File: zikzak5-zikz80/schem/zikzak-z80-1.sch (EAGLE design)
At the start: 3 parts, among them IC1 Z80, IC3 MC6850

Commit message: basic z80 schematic nearly done (missing video and atmega basics like xtal etc)
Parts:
- added BUFFER3: 74LS245N, 74xx-us:74LS245N
- added C1, C2: 0.1uF, SparkFun:CAP0402-CAP
- added C3: (no value), rcl:C-EU025-050X050
- added C4, C6: (no value), rcl:C-EUC0504
- added C5: 10uF, SparkFun:CAP_POL1206
- added IC10, IC11, IC12, IC13, IC15, IC4, IC6: 74LS32N, 74xx-us:74LS32N
- added IC14, IC5, IC7, IC8, IC9: 74LS04N, 74xx-us:74LS04N
- added IC2: ATMEGA644-20PU, atmel:ATMEGA644-20PU
- added JP2: ISP, pinhead:PINHD-1X6
- added LED1, LED3, LED4: (no value), led:LEDMINI-TOP
- added Q1: (no value), adafruit:CRYSTALHC49S
- added R1, R2, R3, R4, R5, R6, R7, R8: (no value), rcl:R-US_0204/2V
- added R10, R11: 2.2K, rcl:R-US_0204/7
- added R12, R13: 10K, rcl:R-US_0204/7
- added R9: (no value), rcl:R-US_0204/7
- added SRAM-128K: CY7C1019CV33-10ZXC, memory-sram:CY7C1019CV33-10ZXC
- added U$1: Z180DIP, skeezix:Z180DIP
- added U$5: PS603SPK, adafruit:PS603SPK
- added U$6: SWITCH-SPST-2TV, SparkFun-Electromechanical:SWITCH-SPST-2TV
- added U$9: Switch, SparkFun-Electromechanical:SWITCH-SPST-2TV
- added U2: FT232RLSSOP, SparkFun:FT232RLSSOP
- added X1, X5: (no value), con-subd:F15HDVS
- added X2: USB-SMD-NS, SparkFun:USB-SMD-NS
- added X3, X4: (no value), con-yamaichi:MD06S
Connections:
- new net +5V: BUFFER3A.DIR
- new net 3.3V: C1.1, U2.3V3OUT
- new net 5V: AT28C256-ROM.VCC, C2.1, C5.+, IC1.VCC, JP2.2, LED1.C, R11.1, R12.2, R13.2, SRAM-128K.+3V@1, SRAM-128K.+3V@2, U2.VCC, U2.VCCIO, X2.VBUS, X4.4
- new net A0: AT28C256-ROM.A0, IC1.A0, IC2.PCINT16/SCL_PC0, SRAM-128K.A0
- new net A1: AT28C256-ROM.A1, IC1.A1, IC2.PCINT17/SDA_PC1, SRAM-128K.A1
- new net A10: AT28C256-ROM.A10, IC1.A10, SRAM-128K.A10
- new net A11: AT28C256-ROM.A11, IC1.A11, SRAM-128K.A11
- new net A12: AT28C256-ROM.A12, SRAM-128K.A12
- new net A13: AT28C256-ROM.A13, IC11A.I1, SRAM-128K.A13
- new net A14: AT28C256-ROM.A14, IC1.A14, IC12A.I1, IC15A.I0, SRAM-128K.A14
- new net A15: IC1.A15, IC13A.I1, SRAM-128K.A15
- new net A2: AT28C256-ROM.A2, IC1.A2, IC2.PCINT18/TCK_PC2, SRAM-128K.A2
- new net A3: AT28C256-ROM.A3, IC1.A3, IC2.PCINT19/TMS_PC3, SRAM-128K.A3
- new net A4: AT28C256-ROM.A4, IC1.A4, SRAM-128K.A4
- new net A5: AT28C256-ROM.A5, IC1.A5, SRAM-128K.A5
- new net A6: AT28C256-ROM.A6, IC1.A6, SRAM-128K.A6
- new net A7: AT28C256-ROM.A7, IC1.A7, SRAM-128K.A7
- new net A8: AT28C256-ROM.A8, IC1.A8, SRAM-128K.A8
- new net A9: AT28C256-ROM.A9, IC1.A9, SRAM-128K.A9
- new net AT_MISO: IC2.PCINT14/MISO_PB6, JP2.1
- new net AT_MOSI: IC2.PCINT13/MOSI_PB5, JP2.4
- new net AT_RESET: IC2.!RESET, JP2.5
- new net AT_SCK: IC2.PCINT15/SCK_PB7, JP2.3
- new net CLK: IC1.CLK, IC9A.O
- new net CPUWANTINT: R13.1
- new net D0: AT28C256-ROM.IO0, IC1.D0, IC2.PCINT0/ADC0_PA0, SRAM-128K.I/O00
- new net D1: AT28C256-ROM.IO1, IC1.D1, IC2.PCINT1/ADC1_PA1, SRAM-128K.I/O01
- new net D2: AT28C256-ROM.IO2, IC1.D2, IC2.PCINT2/ADC2_PA2, SRAM-128K.I/O02
- new net D3: AT28C256-ROM.IO3, IC1.D3, IC2.PCINT3/ADC3_PA3, SRAM-128K.I/O03
- new net D4: AT28C256-ROM.IO4, IC1.D4, IC2.PCINT4/ADC4_PA4, SRAM-128K.I/O04
- new net D5: AT28C256-ROM.IO5, IC1.D5, IC2.PCINT5/ADC5_PA5, SRAM-128K.I/O05
- new net D6: AT28C256-ROM.IO6, IC1.D6, IC2.PCINT6/ADC6_PA6, SRAM-128K.I/O06
- new net D7: AT28C256-ROM.IO7, IC1.D7, IC2.PCINT7/ADC7_PA7, SRAM-128K.I/O07
- new net GND: AT28C256-ROM.GND, C1.2, C2.2, C5.-, IC1.GND, JP2.6, SRAM-128K.A16, SRAM-128K.GND@1, SRAM-128K.GND@2, U$9.P, U2.AGND, U2.CTS, U2.GND18, U2.GND21, U2.GND7, U2.TEST, X2.GND, X4.3
- new net IOREQINT: IC1.IORQ, IC2.PCINT23/TOSC2_PC7
- new net IS_RAM: AT28C256-ROM./CE, IC13A.O, IC14A.I, IC15A.O
- new net IS_READ: AT28C256-ROM./OE, IC4A.O, SRAM-128K.OE
- new net IS_WRITE: IC10A.O, SRAM-128K.WE
- new net KEY_CLOCK: IC2.PCINT22/TOSC1_PC6, X4.5
- new net KEY_DATA: IC2.PCINT21/TDI_PC5, X4.1
- new net MREQ: IC1.MREQ, IC10A.I1, IC4A.I0
- new net N$1: IC11A.O, IC12A.I0
- new net N$105: BUFFER3A.A2
- new net N$106: BUFFER3A.A1
- new net N$109: BUFFER3A.A5
- new net N$11: BUFFER3A.A4
- new net N$110: BUFFER3A.A6
- new net N$111: BUFFER3A.A7
- new net N$112: BUFFER3A.A8
- new net N$113: BUFFER3A.B1, R3.2
- new net N$114: BUFFER3A.B2, R4.2
- new net N$115: BUFFER3A.B3, R5.2
- new net N$116: BUFFER3A.B4, R6.2
- new net N$117: BUFFER3A.B5, R7.2
- new net N$118: BUFFER3A.B6, R8.2
- new net N$119: R3.1, R4.1, X1-1.F
- new net N$12: BUFFER3A.A3
- new net N$121: R5.1, R6.1, X1-2.F
- new net N$122: X1-13.F
- new net N$123: R7.1, R8.1, X1-3.F
- new net N$124: X1-14.F
- new net N$125: BUFFER3A.G
- new net N$2: IC12A.O, IC13A.I0
- new net N$3: IC7A.I, IC8A.O, IC9A.I, R10.2
- new net N$4: IC1.BUSRQ, IC1.NMI, IC1.WAIT, R12.1
- new net N$5: C6.1, IC7A.O
- new net N$6: C6.2, IC8A.I, R10.1
- new net N$7: IC14A.O, SRAM-128K.CE
- new net OPFETCH: IC1.M1, IC2.PCINT20/TDO_PC4
- new net RD: IC1.RD, IC4A.I1
- new net RESETSW: IC1.RESET, R11.2, U$9.O
- new net SER2CPU: IC2.PCINT24/RXD0_PD0, U2.TXD
- new net SERFROMCPU: IC2.PCINT25/TXD0_PD1, U2.RXD
- new net USB_D+: U2.USBDP, X2.D+
- new net USB_D-: U2.USBDM, X2.D-
- new net WR: IC1.WR, IC10A.I0
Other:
- note added: "/"
- note added: "1"
- note added: "14"
- note added: "1K"
- note added: "2"
- note added: "2K"
- note added: "3"
- note added: "4"
- note added: "5"
- note added: "6"
- note added: "7"
- note added: "8"
- note added: "9"
- note added: "Always clear to send (to mcu)"
- note added: "BB"
- note added: "GG"
- note added: "ISP Progr."
- note added: "PS/2 Keyb"
- note added: "RR"
- note added: "Reset Switch - RESET must hold for >3 clock cycles"
- note added: "Serial <-> USB"
- note added: "Single 74LS04 IC 1-2Hz Clock Gen"
- note added: "VGA"
- note added: "http://cpuville.com/images/Z80/schematic_2.GIF"
- moved on the sheet: AT28C256-ROM, IC1, IC3

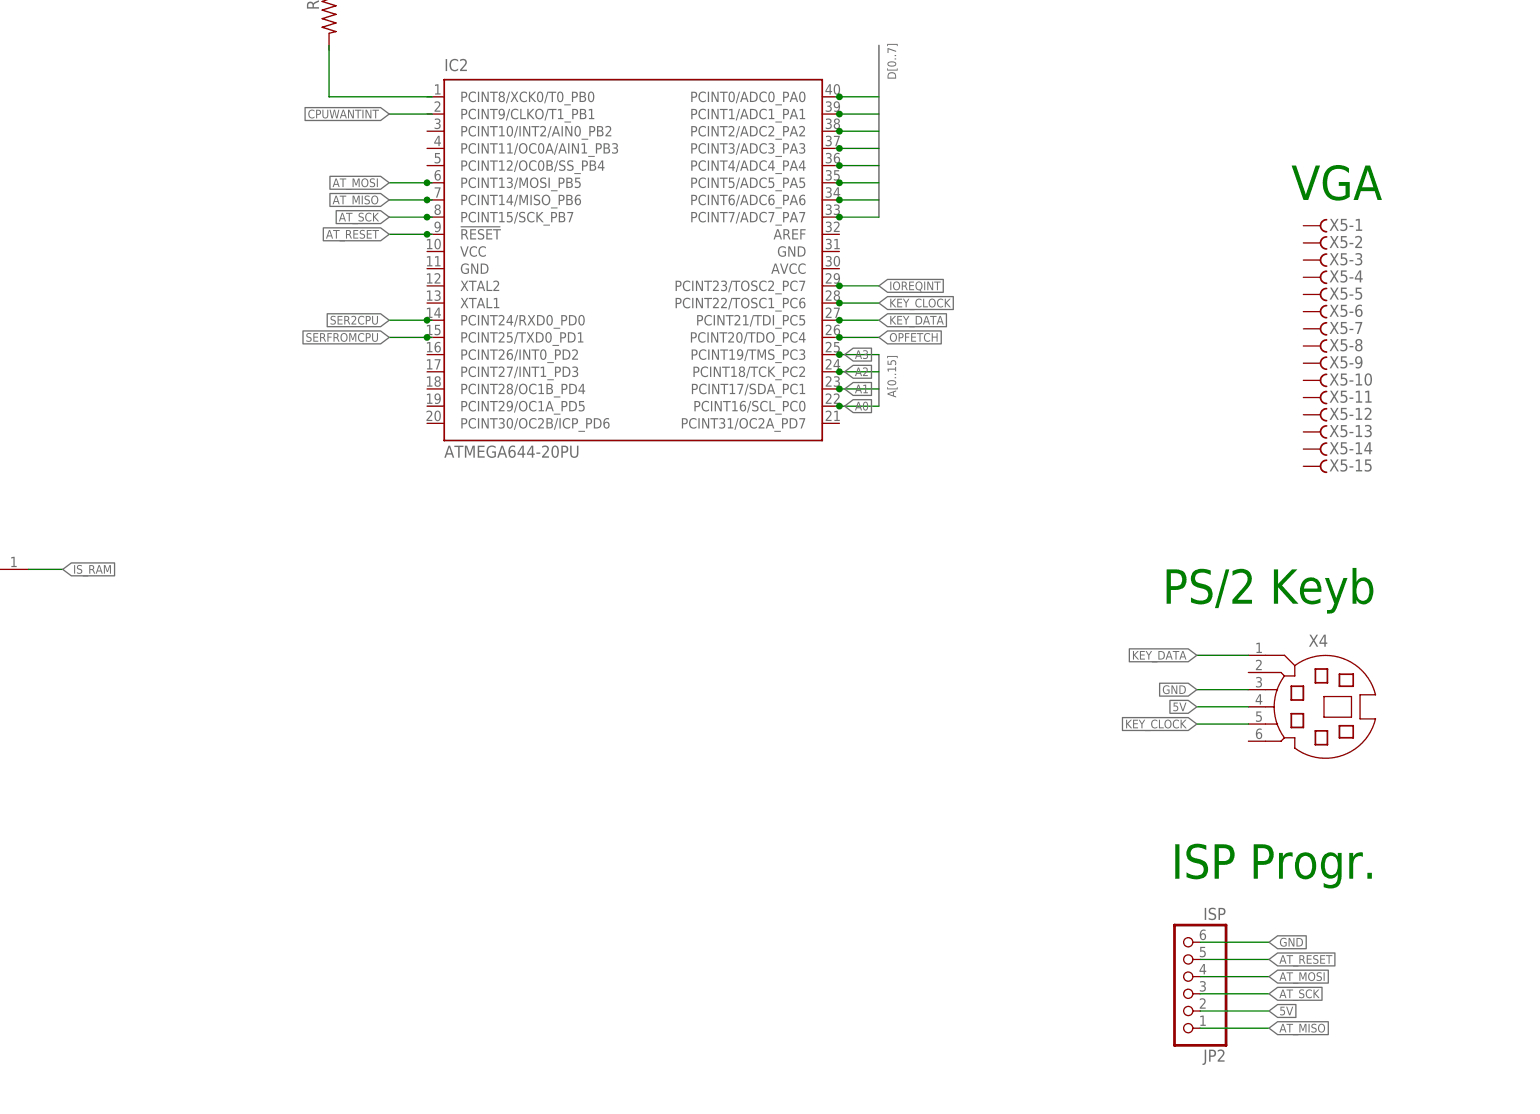
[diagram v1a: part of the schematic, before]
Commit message: Updated schem to complete atmega; added joystick and speaker; populated vga
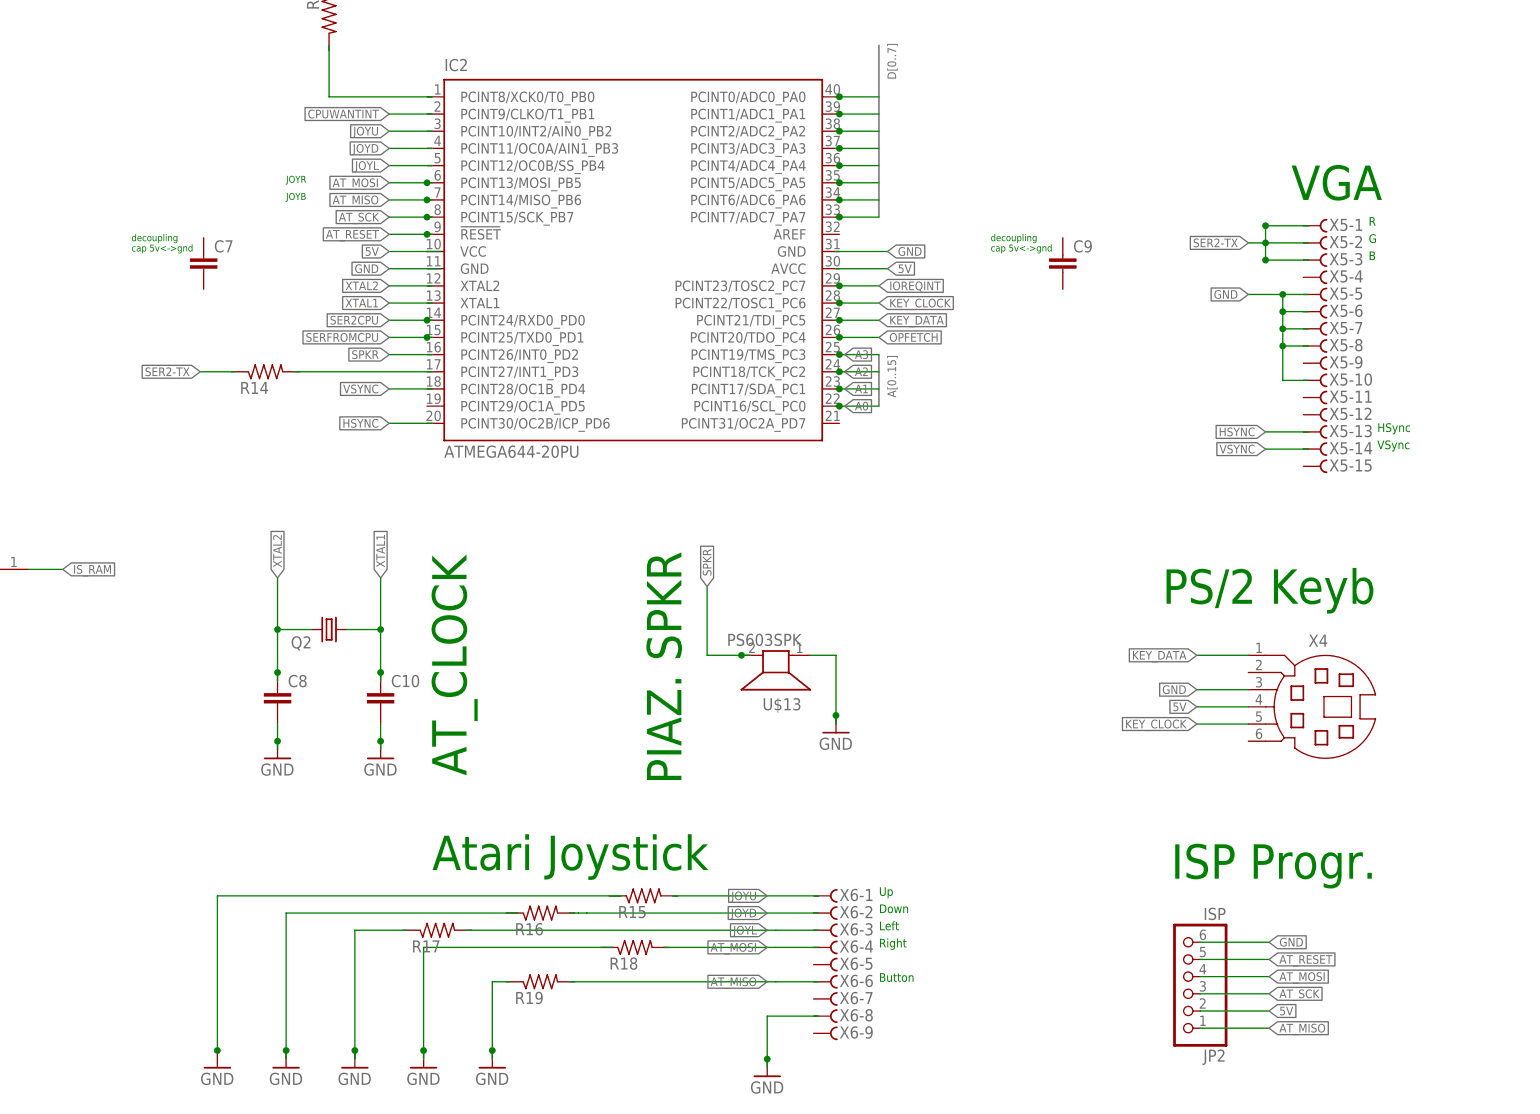
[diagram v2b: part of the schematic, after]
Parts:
- added C10, C7, C8, C9: (no value), rcl:C-EU025-050X050
- added Q2: (no value), adafruit:CRYSTALHC49S
- added R14, R15, R16, R17, R18, R19: (no value), rcl:R-US_0204/2V
- added U$13: PS603SPK, adafruit:PS603SPK
- added X6: (no value), con-subd:F15HDVS
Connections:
- new net SPKR: U$13.2
- new net XTAL1: C10.1, Q2.1
- new net XTAL2: C8.1, Q2.2
- net GND: now also C10.2, C8.2, U$13.1
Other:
- note added: "AT_CLOCK"
- note added: "Atari Joystick"
- note added: "B"
- note added: "Button"
- note added: "Down"
- note added: "G"
- note added: "HSync"
- note added: "JOYB"
- note added: "JOYR"
- note added: "Left"
- note added: "PIAZ. SPKR"
- note added: "R"
- note added: "Right"
- note added: "Up"
- note added: "VSync"
- note added: "decoupling cap 5v<->gnd"

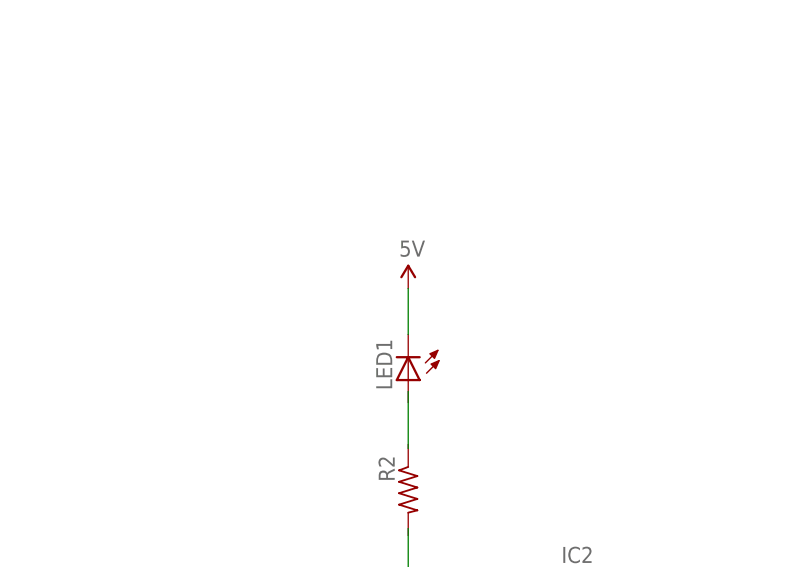
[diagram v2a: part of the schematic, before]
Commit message: Fix, changed a 5v->GND on a LED
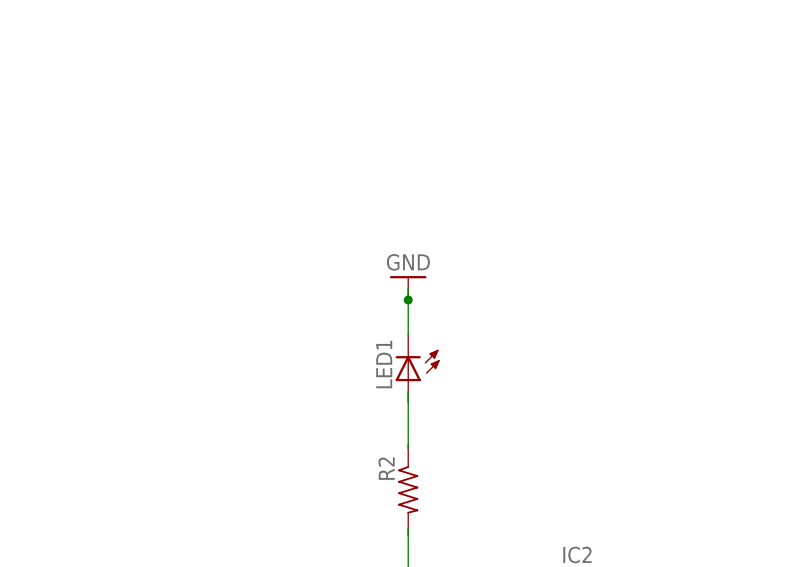
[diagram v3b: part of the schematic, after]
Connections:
- net 5V: no longer LED1.C
- net GND: now also LED1.C
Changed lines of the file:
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@@
 <part name="R1" library="rcl" deviceset="R-US_" device="0204/2V"/>
 <part name="R2" library="rcl" deviceset="R-US_" device="0204/2V"/>
-<part name="U$2" library="SparkFun" deviceset="5V" device=""/>
 <part name="R13" library="rcl" deviceset="R-US_" device="0204/7" value="10K"/>
 <part name="U$4" library="SparkFun" deviceset="5V" device=""/>
@@
 <part name="U$13" library="adafruit" deviceset="PS603" device="SPK"/>
 <part name="GND19" library="SparkFun" deviceset="GND" device=""/>
+<part name="GND20" library="SparkFun" deviceset="GND" device=""/>
 </parts>
 <sheets>
@@
 <instance part="R1" gate="G$1" x="88.138" y="340.36" rot="MR0"/>
 <instance part="R2" gate="G$1" x="369.57" y="164.338" rot="MR270"/>
-<instance part="U$2" gate="G$1" x="369.57" y="186.69"/>
 <instance part="R13" gate="G$1" x="102.87" y="77.47" rot="R270"/>
 <instance part="U$4" gate="G$1" x="102.87" y="68.58" rot="R180"/>
@@
 <instance part="U$13" gate="G$1" x="435.61" y="69.85" rot="R180"/>
 <instance part="GND19" gate="1" x="444.5" y="58.42"/>
+<instance part="GND20" gate="1" x="369.57" y="187.96" rot="R180"/>
 </instances>
 <busses>
@@
 <wire x1="444.5" y1="60.96" x2="444.5" y2="59.69" width="0.1524" layer="91"/>
 <junction x="444.5" y="60.96"/>
+</segment>
+<segment>
+<pinref part="LED1" gate="G$1" pin="C"/>
+<wire x1="369.57" y1="181.61" x2="369.57" y2="185.42" width="0.1524" layer="91"/>
+<pinref part="GND20" gate="1" pin="GND"/>
+<wire x1="369.57" y1="185.42" x2="369.57" y2="186.69" width="0.1524" layer="91"/>
+<junction x="369.57" y="185.42"/>
 </segment>
 </net>
@@
 </segment>
 <segment>
-<pinref part="LED1" gate="G$1" pin="C"/>
-<pinref part="U$2" gate="G$1" pin="5V"/>
-<wire x1="369.57" y1="181.61" x2="369.57" y2="186.69" width="0.1524" layer="91"/>
-</segment>
-<segment>
